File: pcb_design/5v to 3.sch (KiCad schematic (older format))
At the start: 6 parts

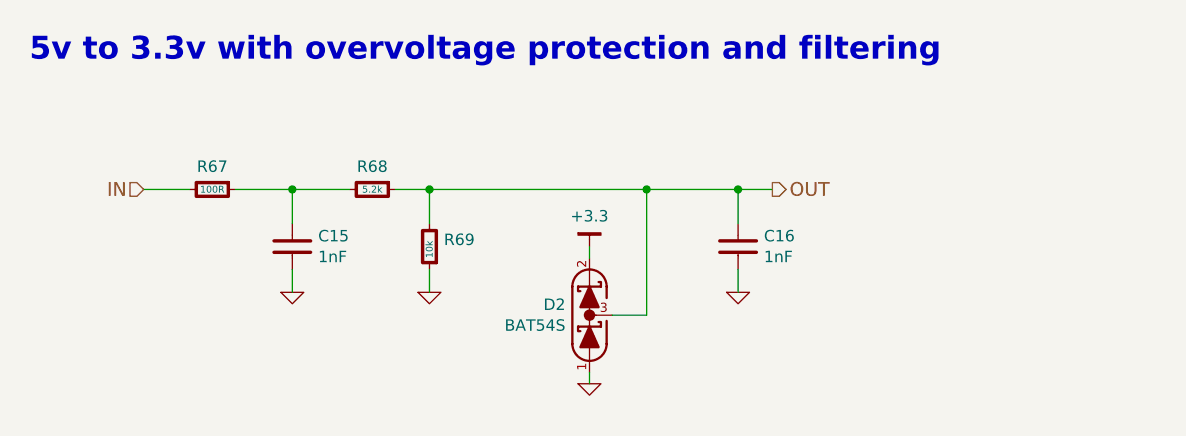
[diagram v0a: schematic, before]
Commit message: Routing complete. Added 3D models. No DRC errors, a few ERC warnings
Signed-off-by: Marcos Chaparro <mchaparro@paltatech.com>
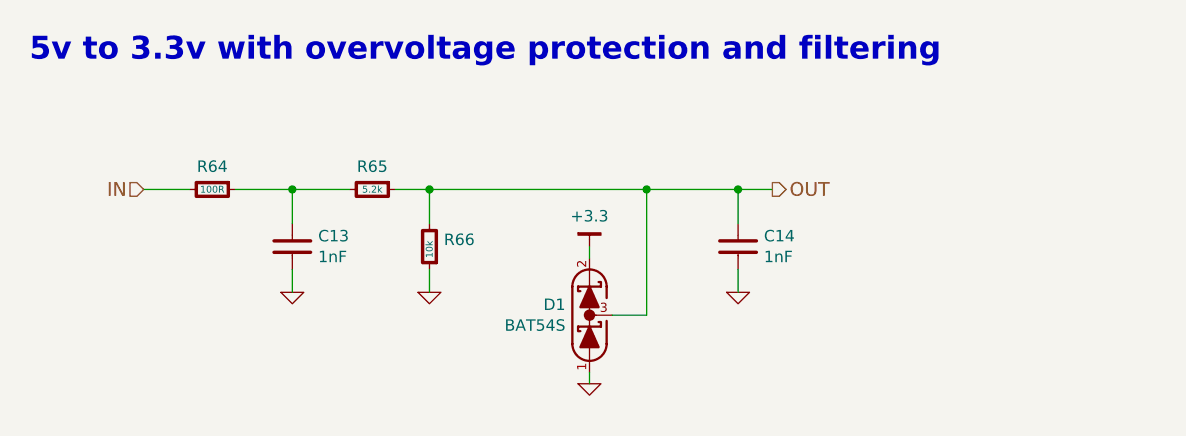
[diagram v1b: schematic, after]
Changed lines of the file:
@@
 AR Path="/5889B2E2/5889F39B" Ref="D1"  Part="1"
 AR Path="/5889CDF9/5889F39B" Ref="D2"  Part="1"
-F 0 "D2" V 5996 4195 50  0000 R CNN
+F 0 "D1" V 5996 4195 50  0000 R CNN
 F 1 "BAT54S" V 5905 4195 50  0000 R CNN
 F 2 "smd-semi:SOT-23" H 5950 4150 60  0001 C CNN
@@
 $EndComp
 $Comp
-L GND #PWR0145
+L GND #PWR0159
 U 1 1 5889F466
 P 5950 4600
-AR Path="/5889B2E2/5889F466" Ref="#PWR0145"  Part="1"
-AR Path="/5889CDF9/5889F466" Ref="#PWR0150"  Part="1"
-F 0 "#PWR0150" H 5950 4600 30  0001 C CNN
+AR Path="/5889B2E2/5889F466" Ref="#PWR0159"  Part="1"
+AR Path="/5889CDF9/5889F466" Ref="#PWR0164"  Part="1"
+F 0 "#PWR0164" H 5950 4600 30  0001 C CNN
 F 1 "GND" H 5950 4530 30  0001 C CNN
 F 2 "" H 5950 4600 60  0000 C CNN
@@
 AR Path="/5889B2E2/5889F74D" Ref="R64"  Part="1"
 AR Path="/5889CDF9/5889F74D" Ref="R67"  Part="1"
-F 0 "R67" V 4200 3750 50  0000 C CNN
+F 0 "R64" V 4200 3750 50  0000 C CNN
 F 1 "100R" V 4300 3750 30  0000 C CNN
 F 2 "IPC7351-Nominal:RESC1608X50" H 4300 3750 50  0001 C CNN
@@
 AR Path="/5889B2E2/5889F796" Ref="R65"  Part="1"
 AR Path="/5889CDF9/5889F796" Ref="R68"  Part="1"
-F 0 "R68" V 4900 3750 50  0000 C CNN
+F 0 "R65" V 4900 3750 50  0000 C CNN
 F 1 "5.2k" V 5000 3750 30  0000 C CNN
 F 2 "IPC7351-Nominal:RESC1608X50" H 5000 3750 50  0001 C CNN
@@
 AR Path="/5889B2E2/5889F7E7" Ref="R66"  Part="1"
 AR Path="/5889CDF9/5889F7E7" Ref="R69"  Part="1"
-F 0 "R69" H 5187 3970 50  0000 R CNN
+F 0 "R66" H 5187 3970 50  0000 R CNN
 F 1 "10k" V 5250 4050 30  0000 R CNN
 F 2 "IPC7351-Nominal:RESC1608X50" H 5250 4000 50  0001 C CNN
@@
 AR Path="/5889B2E2/5889F81D" Ref="C13"  Part="1"
 AR Path="/5889CDF9/5889F81D" Ref="C15"  Part="1"
-F 0 "C15" H 4763 4046 50  0000 L CNN
+F 0 "C13" H 4763 4046 50  0000 L CNN
 F 1 "1nF" H 4763 3955 50  0000 L CNN
 F 2 "IPC7351-Nominal:CAPC1608X55" H 4650 4000 50  0001 C CNN
@@
 $EndComp
 $Comp
-L GND #PWR0146
+L GND #PWR0160
 U 1 1 5889F89D
 P 5250 4200
-AR Path="/5889B2E2/5889F89D" Ref="#PWR0146"  Part="1"
-AR Path="/5889CDF9/5889F89D" Ref="#PWR0151"  Part="1"
-F 0 "#PWR0151" H 5250 4200 30  0001 C CNN
+AR Path="/5889B2E2/5889F89D" Ref="#PWR0160"  Part="1"
+AR Path="/5889CDF9/5889F89D" Ref="#PWR0165"  Part="1"
+F 0 "#PWR0165" H 5250 4200 30  0001 C CNN
 F 1 "GND" H 5250 4130 30  0001 C CNN
 F 2 "" H 5250 4200 60  0000 C CNN
@@
 $EndComp
 $Comp
-L GND #PWR0147
+L GND #PWR0161
 U 1 1 5889F8B7
 P 4650 4200
-AR Path="/5889B2E2/5889F8B7" Ref="#PWR0147"  Part="1"
-AR Path="/5889CDF9/5889F8B7" Ref="#PWR0152"  Part="1"
-F 0 "#PWR0152" H 4650 4200 30  0001 C CNN
+AR Path="/5889B2E2/5889F8B7" Ref="#PWR0161"  Part="1"
+AR Path="/5889CDF9/5889F8B7" Ref="#PWR0166"  Part="1"
+F 0 "#PWR0166" H 4650 4200 30  0001 C CNN
 F 1 "GND" H 4650 4130 30  0001 C CNN
 F 2 "" H 4650 4200 60  0000 C CNN
@@
 AR Path="/5889B2E2/5889FB1A" Ref="C14"  Part="1"
 AR Path="/5889CDF9/5889FB1A" Ref="C16"  Part="1"
-F 0 "C16" H 6713 4046 50  0000 L CNN
+F 0 "C14" H 6713 4046 50  0000 L CNN
 F 1 "1nF" H 6713 3955 50  0000 L CNN
 F 2 "IPC7351-Nominal:CAPC1608X55" H 6600 4000 50  0001 C CNN
@@
 $EndComp
 $Comp
-L GND #PWR0148
+L GND #PWR0162
 U 1 1 5889FBDC
 P 6600 4200
-AR Path="/5889B2E2/5889FBDC" Ref="#PWR0148"  Part="1"
-AR Path="/5889CDF9/5889FBDC" Ref="#PWR0153"  Part="1"
-F 0 "#PWR0153" H 6600 4200 30  0001 C CNN
+AR Path="/5889B2E2/5889FBDC" Ref="#PWR0162"  Part="1"
+AR Path="/5889CDF9/5889FBDC" Ref="#PWR0167"  Part="1"
+F 0 "#PWR0167" H 6600 4200 30  0001 C CNN
 F 1 "GND" H 6600 4130 30  0001 C CNN
 F 2 "" H 6600 4200 60  0000 C CNN
@@
 5v to 3.3v with overvoltage protection and filtering
 $Comp
-L +3.3 #PWR0149
+L +3.3 #PWR0163
 U 1 1 588FFFB4
 P 5950 4000
-AR Path="/5889B2E2/588FFFB4" Ref="#PWR0149"  Part="1"
-AR Path="/5889CDF9/588FFFB4" Ref="#PWR0154"  Part="1"
-F 0 "#PWR0154" H 0   50  30  0001 C CNN
+AR Path="/5889B2E2/588FFFB4" Ref="#PWR0163"  Part="1"
+AR Path="/5889CDF9/588FFFB4" Ref="#PWR0168"  Part="1"
+F 0 "#PWR0168" H 0   50  30  0001 C CNN
 F 1 "+3.3" H 5950 4133 50  0000 C CNN
 F 2 "" H 0   0   60  0000 C CNN

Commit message: Silkscreen logos, fixed swapped OCP inputs, added a button to enter bootloader,missing 3d model.
Signed-off-by: Marcos Chaparro <mchaparro@paltatech.com>
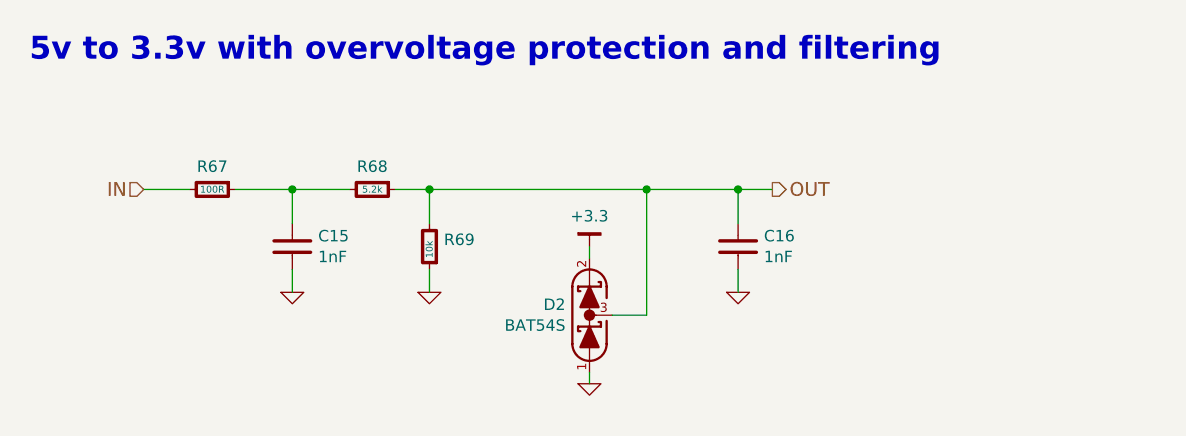
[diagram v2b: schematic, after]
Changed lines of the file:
@@
 AR Path="/5889B2E2/5889F39B" Ref="D1"  Part="1"
 AR Path="/5889CDF9/5889F39B" Ref="D2"  Part="1"
-F 0 "D1" V 5996 4195 50  0000 R CNN
+F 0 "D2" V 5996 4195 50  0000 R CNN
 F 1 "BAT54S" V 5905 4195 50  0000 R CNN
 F 2 "smd-semi:SOT-23" H 5950 4150 60  0001 C CNN
@@
 $EndComp
 $Comp
-L GND #PWR0159
+L GND #PWR168
 U 1 1 5889F466
 P 5950 4600
-AR Path="/5889B2E2/5889F466" Ref="#PWR0159"  Part="1"
-AR Path="/5889CDF9/5889F466" Ref="#PWR0164"  Part="1"
-F 0 "#PWR0164" H 5950 4600 30  0001 C CNN
+AR Path="/5889B2E2/5889F466" Ref="#PWR168"  Part="1"
+AR Path="/5889CDF9/5889F466" Ref="#PWR173"  Part="1"
+F 0 "#PWR173" H 5950 4600 30  0001 C CNN
 F 1 "GND" H 5950 4530 30  0001 C CNN
 F 2 "" H 5950 4600 60  0000 C CNN
@@
 AR Path="/5889B2E2/5889F74D" Ref="R64"  Part="1"
 AR Path="/5889CDF9/5889F74D" Ref="R67"  Part="1"
-F 0 "R64" V 4200 3750 50  0000 C CNN
+F 0 "R67" V 4200 3750 50  0000 C CNN
 F 1 "100R" V 4300 3750 30  0000 C CNN
 F 2 "IPC7351-Nominal:RESC1608X50" H 4300 3750 50  0001 C CNN
@@
 AR Path="/5889B2E2/5889F796" Ref="R65"  Part="1"
 AR Path="/5889CDF9/5889F796" Ref="R68"  Part="1"
-F 0 "R65" V 4900 3750 50  0000 C CNN
+F 0 "R68" V 4900 3750 50  0000 C CNN
 F 1 "5.2k" V 5000 3750 30  0000 C CNN
 F 2 "IPC7351-Nominal:RESC1608X50" H 5000 3750 50  0001 C CNN
@@
 AR Path="/5889B2E2/5889F7E7" Ref="R66"  Part="1"
 AR Path="/5889CDF9/5889F7E7" Ref="R69"  Part="1"
-F 0 "R66" H 5187 3970 50  0000 R CNN
+F 0 "R69" H 5187 3970 50  0000 R CNN
 F 1 "10k" V 5250 4050 30  0000 R CNN
 F 2 "IPC7351-Nominal:RESC1608X50" H 5250 4000 50  0001 C CNN
@@
 AR Path="/5889B2E2/5889F81D" Ref="C13"  Part="1"
 AR Path="/5889CDF9/5889F81D" Ref="C15"  Part="1"
-F 0 "C13" H 4763 4046 50  0000 L CNN
+F 0 "C15" H 4763 4046 50  0000 L CNN
 F 1 "1nF" H 4763 3955 50  0000 L CNN
 F 2 "IPC7351-Nominal:CAPC1608X55" H 4650 4000 50  0001 C CNN
@@
 $EndComp
 $Comp
-L GND #PWR0160
+L GND #PWR166
 U 1 1 5889F89D
 P 5250 4200
-AR Path="/5889B2E2/5889F89D" Ref="#PWR0160"  Part="1"
-AR Path="/5889CDF9/5889F89D" Ref="#PWR0165"  Part="1"
-F 0 "#PWR0165" H 5250 4200 30  0001 C CNN
+AR Path="/5889B2E2/5889F89D" Ref="#PWR166"  Part="1"
+AR Path="/5889CDF9/5889F89D" Ref="#PWR171"  Part="1"
+F 0 "#PWR171" H 5250 4200 30  0001 C CNN
 F 1 "GND" H 5250 4130 30  0001 C CNN
 F 2 "" H 5250 4200 60  0000 C CNN
@@
 $EndComp
 $Comp
-L GND #PWR0161
+L GND #PWR165
 U 1 1 5889F8B7
 P 4650 4200
-AR Path="/5889B2E2/5889F8B7" Ref="#PWR0161"  Part="1"
-AR Path="/5889CDF9/5889F8B7" Ref="#PWR0166"  Part="1"
-F 0 "#PWR0166" H 4650 4200 30  0001 C CNN
+AR Path="/5889B2E2/5889F8B7" Ref="#PWR165"  Part="1"
+AR Path="/5889CDF9/5889F8B7" Ref="#PWR170"  Part="1"
+F 0 "#PWR170" H 4650 4200 30  0001 C CNN
 F 1 "GND" H 4650 4130 30  0001 C CNN
 F 2 "" H 4650 4200 60  0000 C CNN
@@
 AR Path="/5889B2E2/5889FB1A" Ref="C14"  Part="1"
 AR Path="/5889CDF9/5889FB1A" Ref="C16"  Part="1"
-F 0 "C14" H 6713 4046 50  0000 L CNN
+F 0 "C16" H 6713 4046 50  0000 L CNN
 F 1 "1nF" H 6713 3955 50  0000 L CNN
 F 2 "IPC7351-Nominal:CAPC1608X55" H 6600 4000 50  0001 C CNN
@@
 $EndComp
 $Comp
-L GND #PWR0162
+L GND #PWR169
 U 1 1 5889FBDC
 P 6600 4200
-AR Path="/5889B2E2/5889FBDC" Ref="#PWR0162"  Part="1"
-AR Path="/5889CDF9/5889FBDC" Ref="#PWR0167"  Part="1"
-F 0 "#PWR0167" H 6600 4200 30  0001 C CNN
+AR Path="/5889B2E2/5889FBDC" Ref="#PWR169"  Part="1"
+AR Path="/5889CDF9/5889FBDC" Ref="#PWR174"  Part="1"
+F 0 "#PWR174" H 6600 4200 30  0001 C CNN
 F 1 "GND" H 6600 4130 30  0001 C CNN
 F 2 "" H 6600 4200 60  0000 C CNN
@@
 5v to 3.3v with overvoltage protection and filtering
 $Comp
-L +3.3 #PWR0163
+L +3.3 #PWR167
 U 1 1 588FFFB4
 P 5950 4000
-AR Path="/5889B2E2/588FFFB4" Ref="#PWR0163"  Part="1"
-AR Path="/5889CDF9/588FFFB4" Ref="#PWR0168"  Part="1"
-F 0 "#PWR0168" H 0   50  30  0001 C CNN
+AR Path="/5889B2E2/588FFFB4" Ref="#PWR167"  Part="1"
+AR Path="/5889CDF9/588FFFB4" Ref="#PWR172"  Part="1"
+F 0 "#PWR172" H 0   50  30  0001 C CNN
 F 1 "+3.3" H 5950 4133 50  0000 C CNN
 F 2 "" H 0   0   60  0000 C CNN

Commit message: Updated component values according to simulations. 1.5khz for user inputs and  240khz lp pass filters for motor control
Signed-off-by: Marcos Chaparro <mchaparro@paltatech.com>
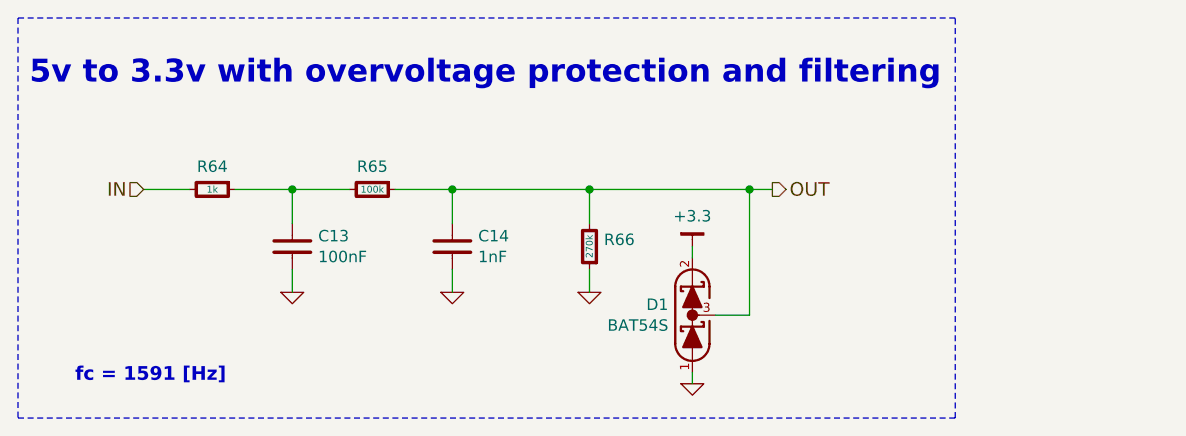
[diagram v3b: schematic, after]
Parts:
- C13: value 1nF -> 100nF; BOM CAP MLCC 100pF C0G 50V 5% [0603] -> CAP MLCC 4.7nF X7R 50V 10% [0603]; mfg# (none) -> GRM188R71H472KA01D
- C14: BOM CAP MLCC 100pF C0G 50V 5% [0603] -> CAP MLCC 4.7nF X7R 50V 10% [0603]; mfg# (none) -> GRM188R71H472KA01D
- D1: mfg# (none) -> TBAT54S,LM
- R64: value 100R -> 1k
- R65: value 5.2k -> 100k; BOM RES SMD 1k 5% [0603] -> RES SMD 100k 1% [0603]
- R66: value 10k -> 270k
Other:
- note added: "fc = 1591 [Hz]"
- moved on the sheet: C14, D1, R66

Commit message: Completed some part numbers
Signed-off-by: Marcos Chaparro <mchaparro@paltatech.com>
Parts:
- C13: MFR (none) -> Murata Electronics North America; MPN (none) -> GRM188R71E104KA01D; SPN (none) -> 490-1524-1-ND; SPR (none) -> Digikey
- C14: BOM CAP MLCC 4.7nF X7R 50V 10% [0603] -> CAP MLCC 1nF X7R 50V 10% [0603]; MFR (none) -> Murata Electronics North America; MPN (none) -> GRM188R71H102KA01D; SPN (none) -> 490-1494-1-ND; SPR (none) -> Digikey; mfg# GRM188R71H472KA01D -> (none)

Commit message: Completed part number, manufacturer, etc fields. Simulated analog conditioning
Signed-off-by: Marcos Chaparro <mchaparro@paltatech.com>
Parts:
- D1: MFR (none) -> Toshiba Semiconductor and Storage; MPN (none) -> TBAT54S,LM; SPN (none) -> TBAT54SLMCT-ND; SPR (none) -> Digikey
- R64: MFR (none) -> Yageo; MPN (none) -> RC0603FR-071KL; SPN (none) -> 311-1.00KHRCT-ND; SPR (none) -> Digikey
- R65: MFR (none) -> Yageo; MPN (none) -> RC0603FR-07100KL; SPN (none) -> 311-100KHRCT-ND; SPR (none) -> Digikey
- R66: MFR (none) -> Yageo; MPN (none) -> RC0603FR-07270KL; SPN (none) -> 311-270KHRCT-ND; SPR (none) -> Digikey
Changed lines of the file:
@@
 F 1 "BAT54S" V 6355 4195 50 0000 R CNN
 F 2 "smd-semi:SOT-23" H 6400 4150 60 0001 C CNN
-F 3 "" V 6350 4300 60 0000 C CNN
+F 3 "http://toshiba.semicon-storage.com/info/docget.jsp?did=37137&prodName=TBAT54" V 6350 4300 60 0001 C CNN
 F 4 "TBAT54S,LM" H 6400 4300 60 0001 C CNN "mfg#"
 F 5 "SCHOTTKY BAT54S" H 6400 4050 60 0001 C CNN "BOM"
-F 6 "" H 0 0 50 0001 C CNN "MFR"
-F 7 "" H 0 0 50 0001 C CNN "MPN"
-F 8 "" H 0 0 50 0001 C CNN "SPR"
-F 9 "" H 0 0 50 0001 C CNN "SPN"
+F 6 "Toshiba Semiconductor and Storage" H 0 0 50 0001 C CNN "MFR"
+F 7 "TBAT54S,LM" H 0 0 50 0001 C CNN "MPN"
+F 8 "Digikey" H 0 0 50 0001 C CNN "SPR"
+F 9 "TBAT54SLMCT-ND" H 0 0 50 0001 C CNN "SPN"
 F 10 "" H 0 0 50 0001 C CNN "SPURL"
 	1    6400 4300
@@
 F 1 "1k" V 4300 3750 30 0000 C CNN
 F 2 "IPC7351-Nominal:RESC1608X50" H 4300 3750 50 0001 C CNN
-F 3 "" H 4300 3800 60 0000 C CNN
+F 3 "" H 4300 3800 60 0001 C CNN
 F 4 "RES SMD 1k 5% [0603]" H 5050 4300 60 0001 C CNN "BOM"
-F 5 "" H 0 0 50 0001 C CNN "MFR"
-F 6 "" H 0 0 50 0001 C CNN "MPN"
-F 7 "" H 0 0 50 0001 C CNN "SPR"
-F 8 "" H 0 0 50 0001 C CNN "SPN"
+F 5 "Yageo" H 0 0 50 0001 C CNN "MFR"
+F 6 "RC0603FR-071KL" H 0 0 50 0001 C CNN "MPN"
+F 7 "Digikey" H 0 0 50 0001 C CNN "SPR"
+F 8 "311-1.00KHRCT-ND" H 0 0 50 0001 C CNN "SPN"
 F 9 "" H 0 0 50 0001 C CNN "SPURL"
 	1    4300 3750
@@
 F 1 "100k" V 5000 3750 30 0000 C CNN
 F 2 "IPC7351-Nominal:RESC1608X50" H 5000 3750 50 0001 C CNN
-F 3 "" H 5000 3800 60 0000 C CNN
+F 3 "http://www.yageo.com/NewPortal/yageodocoutput?fileName=/pdf/R-Chip/PYu-RC_Group_51_RoHS_L_4.pdf" H 5000 3800 60 0001 C CNN
 F 4 "RES SMD 100k 1% [0603]" H 5750 4300 60 0001 C CNN "BOM"
-F 5 "" H 0 0 50 0001 C CNN "MFR"
-F 6 "" H 0 0 50 0001 C CNN "MPN"
-F 7 "" H 0 0 50 0001 C CNN "SPR"
-F 8 "" H 0 0 50 0001 C CNN "SPN"
+F 5 "Yageo" H 0 0 50 0001 C CNN "MFR"
+F 6 "RC0603FR-07100KL" H 0 0 50 0001 C CNN "MPN"
+F 7 "Digikey" H 0 0 50 0001 C CNN "SPR"
+F 8 "311-100KHRCT-ND" H 0 0 50 0001 C CNN "SPN"
 F 9 "" H 0 0 50 0001 C CNN "SPURL"
 	1    5000 3750
@@
 F 1 "270k" V 5950 4050 30 0000 R CNN
 F 2 "IPC7351-Nominal:RESC1608X50" H 5950 4000 50 0001 C CNN
-F 3 "" H 5950 4050 60 0000 C CNN
+F 3 "" H 5950 4050 60 0001 C CNN
 F 4 "RES SMD 1k 5% [0603]" H 6700 4550 60 0001 C CNN "BOM"
-F 5 "" H 0 0 50 0001 C CNN "MFR"
-F 6 "" H 0 0 50 0001 C CNN "MPN"
-F 7 "" H 0 0 50 0001 C CNN "SPR"
-F 8 "" H 0 0 50 0001 C CNN "SPN"
+F 5 "Yageo" H 0 0 50 0001 C CNN "MFR"
+F 6 "RC0603FR-07270KL" H 0 0 50 0001 C CNN "MPN"
+F 7 "Digikey" H 0 0 50 0001 C CNN "SPR"
+F 8 "311-270KHRCT-ND" H 0 0 50 0001 C CNN "SPN"
 F 9 "" H 0 0 50 0001 C CNN "SPURL"
 	1    5950 4000

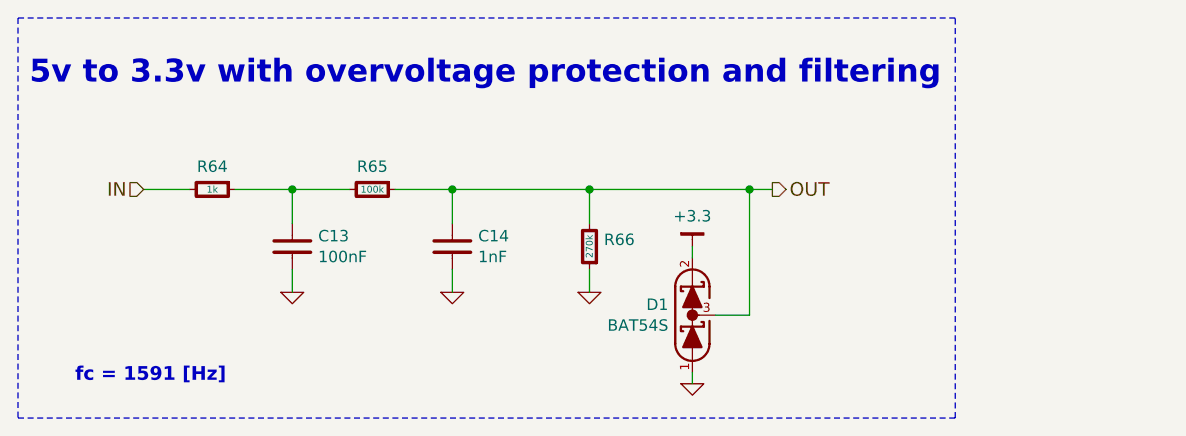
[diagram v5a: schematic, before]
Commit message: Corrected phase current gain. More 3d models
Signed-off-by: Marcos Chaparro <mchaparro@paltatech.com>
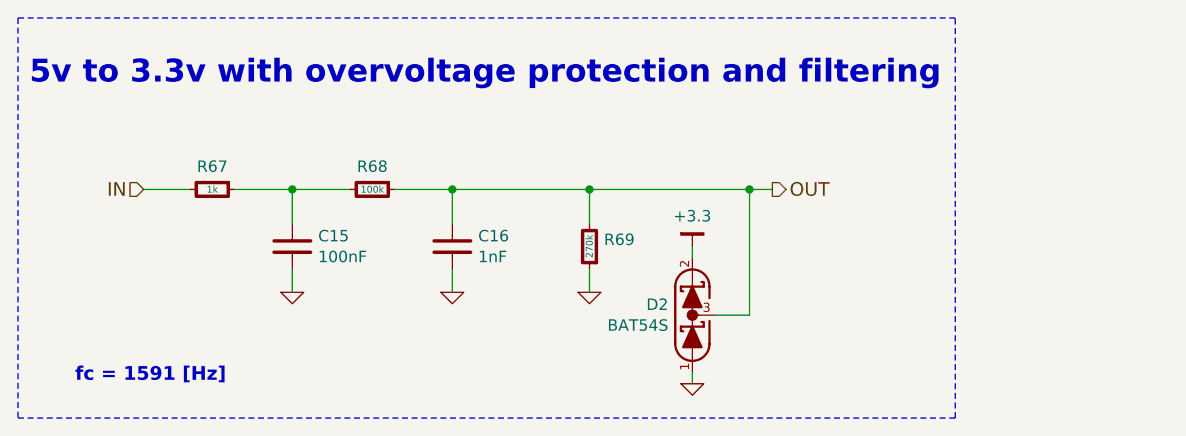
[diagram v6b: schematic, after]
